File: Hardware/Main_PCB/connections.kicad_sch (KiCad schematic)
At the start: 6 parts, among them J701 Conn_01x08_Pin, J702 Conn_01x03_Pin, J703 Servo con, U701 NRF24L01, U702 SN74LV1T34DBV

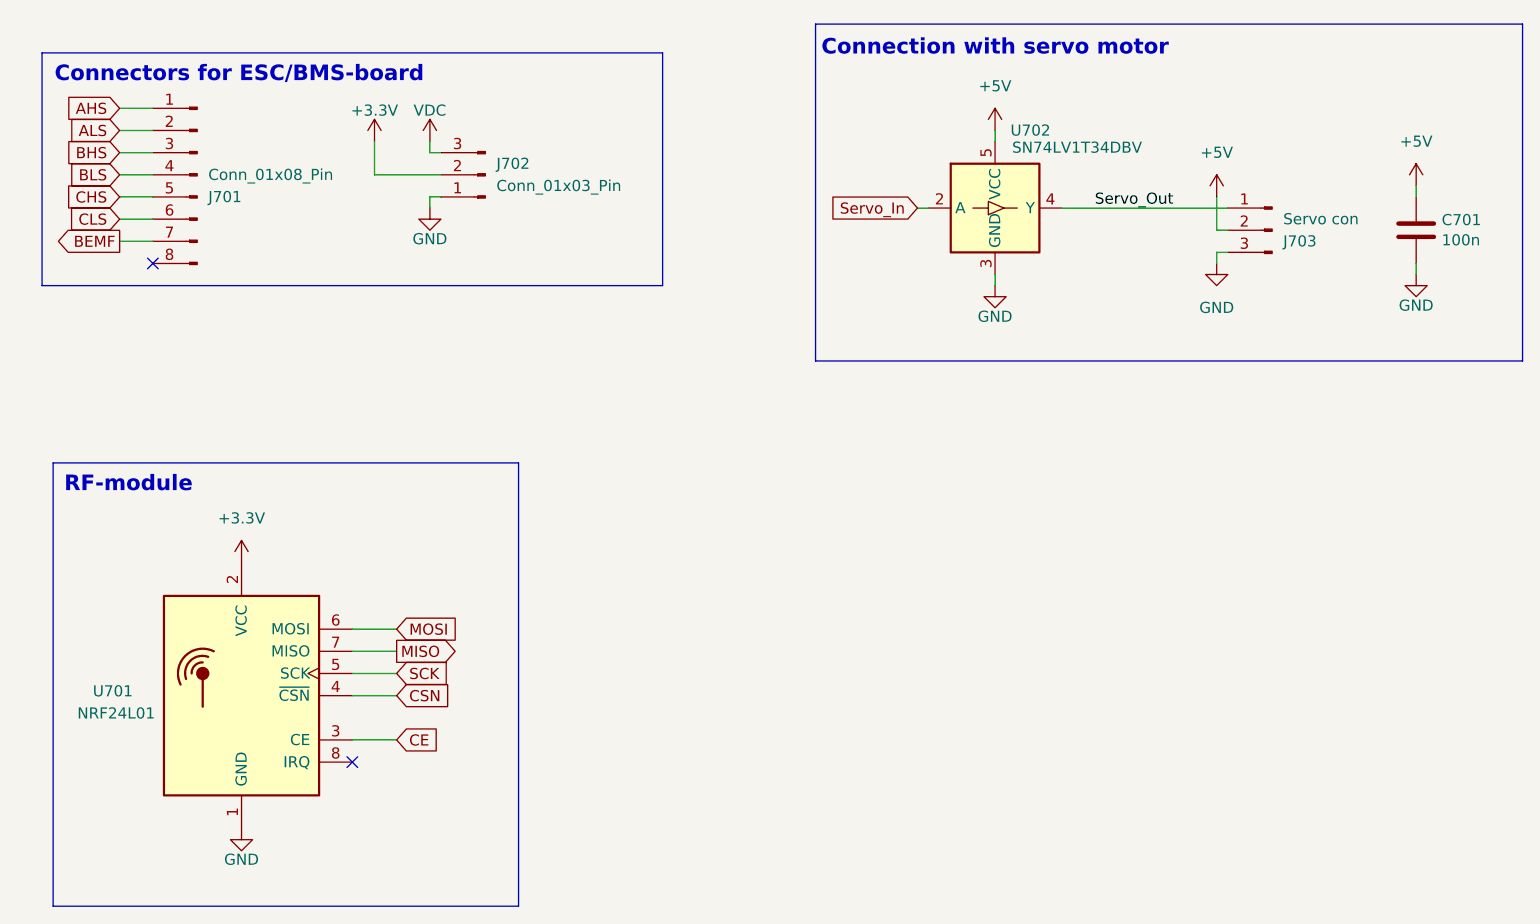
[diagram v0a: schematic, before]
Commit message: Added footprints to all components
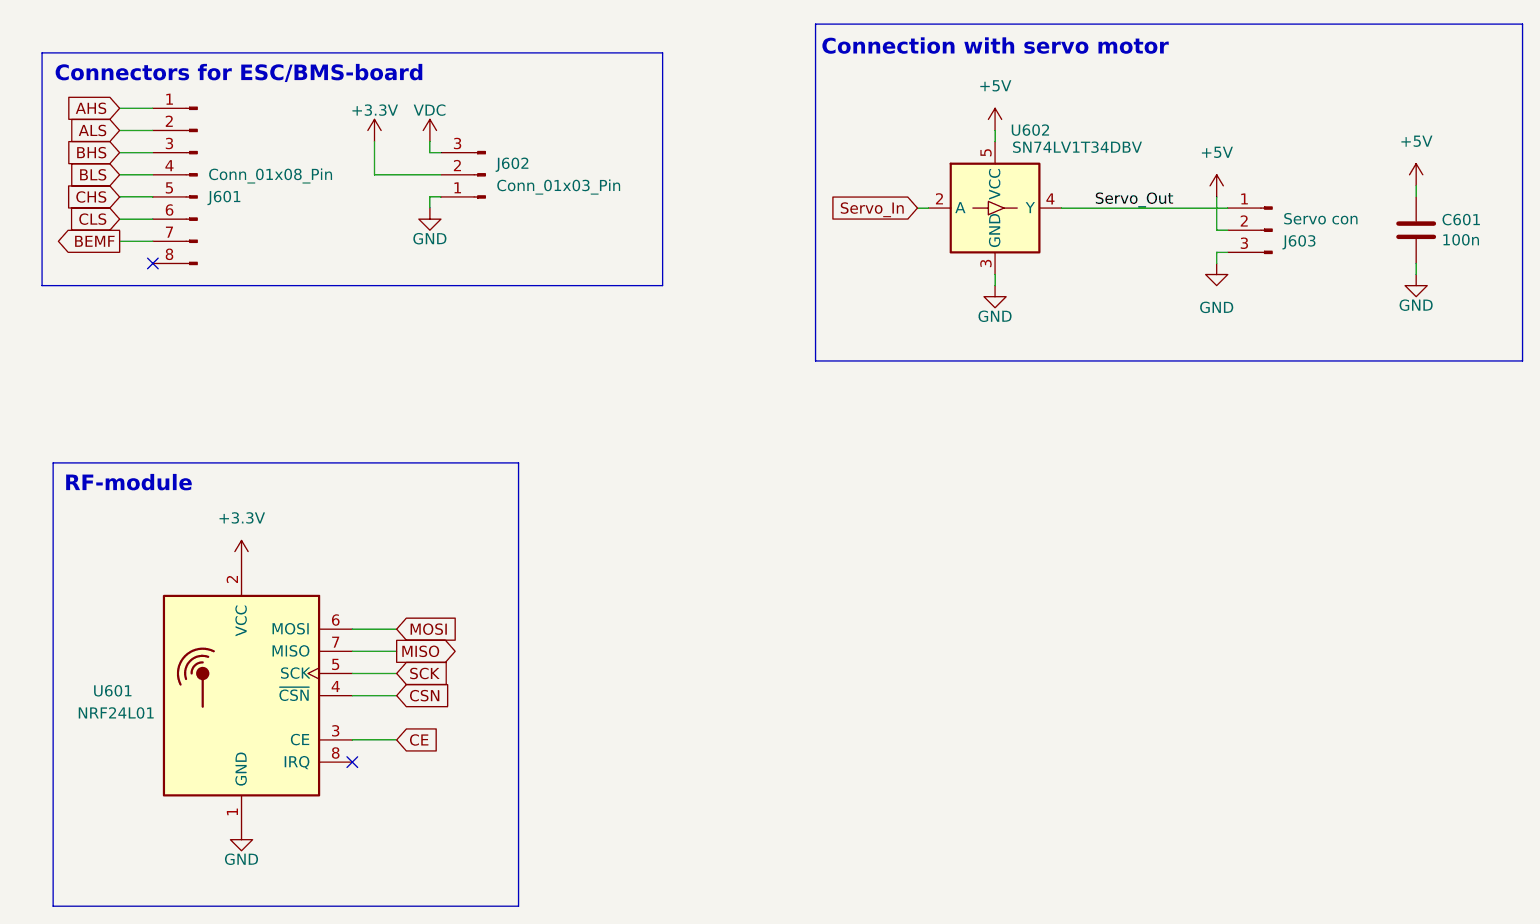
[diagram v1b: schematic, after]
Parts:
- renumbered C701 to C601, J701 to J601, J702 to J602, J703 to J603, U701 to U601, U702 to U602
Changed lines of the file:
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@@
 		(on_board yes)
 		(dnp no)
-		(property "Reference" "#PWR0707"
+		(property "Reference" "#PWR0607"
 			(at 130.81 54.61 0)
 			(effects
@@
 			(project "Main_PCB"
 				(path "/90d7beec-e1a2-46f8-bbb2-6b8f3489db10/2fd609f6-122d-440e-b3d6-5f283f47ac3b"
-					(reference "#PWR0707")
+					(reference "#PWR0607")
 					(unit 1)
 				)
@@
 		(dnp no)
 		(fields_autoplaced yes)
-		(property "Reference" "#PWR0709"
+		(property "Reference" "#PWR0609"
 			(at 156.21 52.07 0)
 			(effects
@@
 			(project "Main_PCB"
 				(path "/90d7beec-e1a2-46f8-bbb2-6b8f3489db10/2fd609f6-122d-440e-b3d6-5f283f47ac3b"
-					(reference "#PWR0709")
+					(reference "#PWR0609")
 					(unit 1)
 				)
@@
 		(dnp no)
 		(fields_autoplaced yes)
-		(property "Reference" "#PWR0710"
+		(property "Reference" "#PWR0610"
 			(at 179.07 40.64 0)
 			(effects
@@
 			(project "Main_PCB"
 				(path "/90d7beec-e1a2-46f8-bbb2-6b8f3489db10/2fd609f6-122d-440e-b3d6-5f283f47ac3b"
-					(reference "#PWR0710")
+					(reference "#PWR0610")
 					(unit 1)
 				)
@@
 		(on_board yes)
 		(dnp no)
-		(property "Reference" "J701"
+		(property "Reference" "J601"
 			(at 40.64 38.1001 0)
 			(effects
@@
 			(project "Main_PCB"
 				(path "/90d7beec-e1a2-46f8-bbb2-6b8f3489db10/2fd609f6-122d-440e-b3d6-5f283f47ac3b"
-					(reference "J701")
+					(reference "J601")
 					(unit 1)
 				)
@@
 		(on_board yes)
 		(dnp no)
-		(property "Reference" "U701"
+		(property "Reference" "U601"
 			(at 32.004 94.742 0)
 			(effects
@@
 			(project "Main_PCB"
 				(path "/90d7beec-e1a2-46f8-bbb2-6b8f3489db10/2fd609f6-122d-440e-b3d6-5f283f47ac3b"
-					(reference "U701")
+					(reference "U601")
 					(unit 1)
 				)
@@
 		(on_board yes)
 		(dnp no)
-		(property "Reference" "#PWR0702"
+		(property "Reference" "#PWR0602"
 			(at 44.45 116.84 0)
 			(effects
@@
 			(project "Main_PCB"
 				(path "/90d7beec-e1a2-46f8-bbb2-6b8f3489db10/2fd609f6-122d-440e-b3d6-5f283f47ac3b"
-					(reference "#PWR0702")
+					(reference "#PWR0602")
 					(unit 1)
 				)
@@
 		(on_board yes)
 		(dnp no)
-		(property "Reference" "#PWR0705"
+		(property "Reference" "#PWR0605"
 			(at 66.04 45.72 0)
 			(effects
@@
 			(project "Main_PCB"
 				(path "/90d7beec-e1a2-46f8-bbb2-6b8f3489db10/2fd609f6-122d-440e-b3d6-5f283f47ac3b"
-					(reference "#PWR0705")
+					(reference "#PWR0605")
 					(unit 1)
 				)
@@
 		(on_board yes)
 		(dnp no)
-		(property "Reference" "U702"
+		(property "Reference" "U602"
 			(at 134.874 30.48 0)
 			(effects
@@
 			(project "Main_PCB"
 				(path "/90d7beec-e1a2-46f8-bbb2-6b8f3489db10/2fd609f6-122d-440e-b3d6-5f283f47ac3b"
-					(reference "U702")
+					(reference "U602")
 					(unit 1)
 				)
@@
 		(on_board yes)
 		(dnp no)
-		(property "Reference" "C701"
+		(property "Reference" "C601"
 			(at 181.991 40.7416 0)
 			(effects
@@
 			(project "Main_PCB"
 				(path "/90d7beec-e1a2-46f8-bbb2-6b8f3489db10/2fd609f6-122d-440e-b3d6-5f283f47ac3b"
-					(reference "C701")
+					(reference "C601")
 					(unit 1)
 				)
@@
 		(on_board yes)
 		(dnp no)
-		(property "Reference" "#PWR0704"
+		(property "Reference" "#PWR0604"
 			(at 66.04 35.56 0)
 			(effects
@@
 			(project "Main_PCB"
 				(path "/90d7beec-e1a2-46f8-bbb2-6b8f3489db10/2fd609f6-122d-440e-b3d6-5f283f47ac3b"
-					(reference "#PWR0704")
+					(reference "#PWR0604")
 					(unit 1)
 				)
@@
 		(on_board yes)
 		(dnp no)
-		(property "Reference" "J703"
+		(property "Reference" "J603"
 			(at 163.83 43.1801 0)
 			(effects
@@
 			(project "Main_PCB"
 				(path "/90d7beec-e1a2-46f8-bbb2-6b8f3489db10/2fd609f6-122d-440e-b3d6-5f283f47ac3b"
-					(reference "J703")
+					(reference "J603")
 					(unit 1)
 				)
@@
 		(dnp no)
 		(fields_autoplaced yes)
-		(property "Reference" "#PWR0701"
+		(property "Reference" "#PWR0601"
 			(at 44.45 83.82 0)
 			(effects
@@
 			(project "Main_PCB"
 				(path "/90d7beec-e1a2-46f8-bbb2-6b8f3489db10/2fd609f6-122d-440e-b3d6-5f283f47ac3b"
-					(reference "#PWR0701")
+					(reference "#PWR0601")
 					(unit 1)
 				)
@@
 		(dnp no)
 		(fields_autoplaced yes)
-		(property "Reference" "#PWR0708"
+		(property "Reference" "#PWR0608"
 			(at 156.21 41.91 0)
 			(effects
@@
 			(project "Main_PCB"
 				(path "/90d7beec-e1a2-46f8-bbb2-6b8f3489db10/2fd609f6-122d-440e-b3d6-5f283f47ac3b"
-					(reference "#PWR0708")
+					(reference "#PWR0608")
 					(unit 1)
 				)
@@
 		(dnp no)
 		(fields_autoplaced yes)
-		(property "Reference" "#PWR0706"
+		(property "Reference" "#PWR0606"
 			(at 130.81 34.29 0)
 			(effects
@@
 			(project "Main_PCB"
 				(path "/90d7beec-e1a2-46f8-bbb2-6b8f3489db10/2fd609f6-122d-440e-b3d6-5f283f47ac3b"
-					(reference "#PWR0706")
+					(reference "#PWR0606")
 					(unit 1)
 				)
@@
 		(on_board yes)
 		(dnp no)
-		(property "Reference" "#PWR0703"
+		(property "Reference" "#PWR0603"
 			(at 59.69 35.56 0)
 			(effects
@@
 			(project "Main_PCB"
 				(path "/90d7beec-e1a2-46f8-bbb2-6b8f3489db10/2fd609f6-122d-440e-b3d6-5f283f47ac3b"
-					(reference "#PWR0703")
+					(reference "#PWR0603")
 					(unit 1)
 				)
@@
 		(on_board yes)
 		(dnp no)
-		(property "Reference" "#PWR0711"
+		(property "Reference" "#PWR0611"
 			(at 179.07 53.34 0)
 			(effects
@@
 			(project "Main_PCB"
 				(path "/90d7beec-e1a2-46f8-bbb2-6b8f3489db10/2fd609f6-122d-440e-b3d6-5f283f47ac3b"
-					(reference "#PWR0711")
+					(reference "#PWR0611")
 					(unit 1)
 				)
@@
 		(dnp no)
 		(fields_autoplaced yes)
-		(property "Reference" "J702"
+		(property "Reference" "J602"
 			(at 73.66 34.2899 0)
 			(effects
@@
 			(project "Main_PCB"
 				(path "/90d7beec-e1a2-46f8-bbb2-6b8f3489db10/2fd609f6-122d-440e-b3d6-5f283f47ac3b"
-					(reference "J702")
-					(unit 1)
-				)
+					(reference "J602")
+					(unit 1)
+				)

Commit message: Finished the schematic of the MainPCB
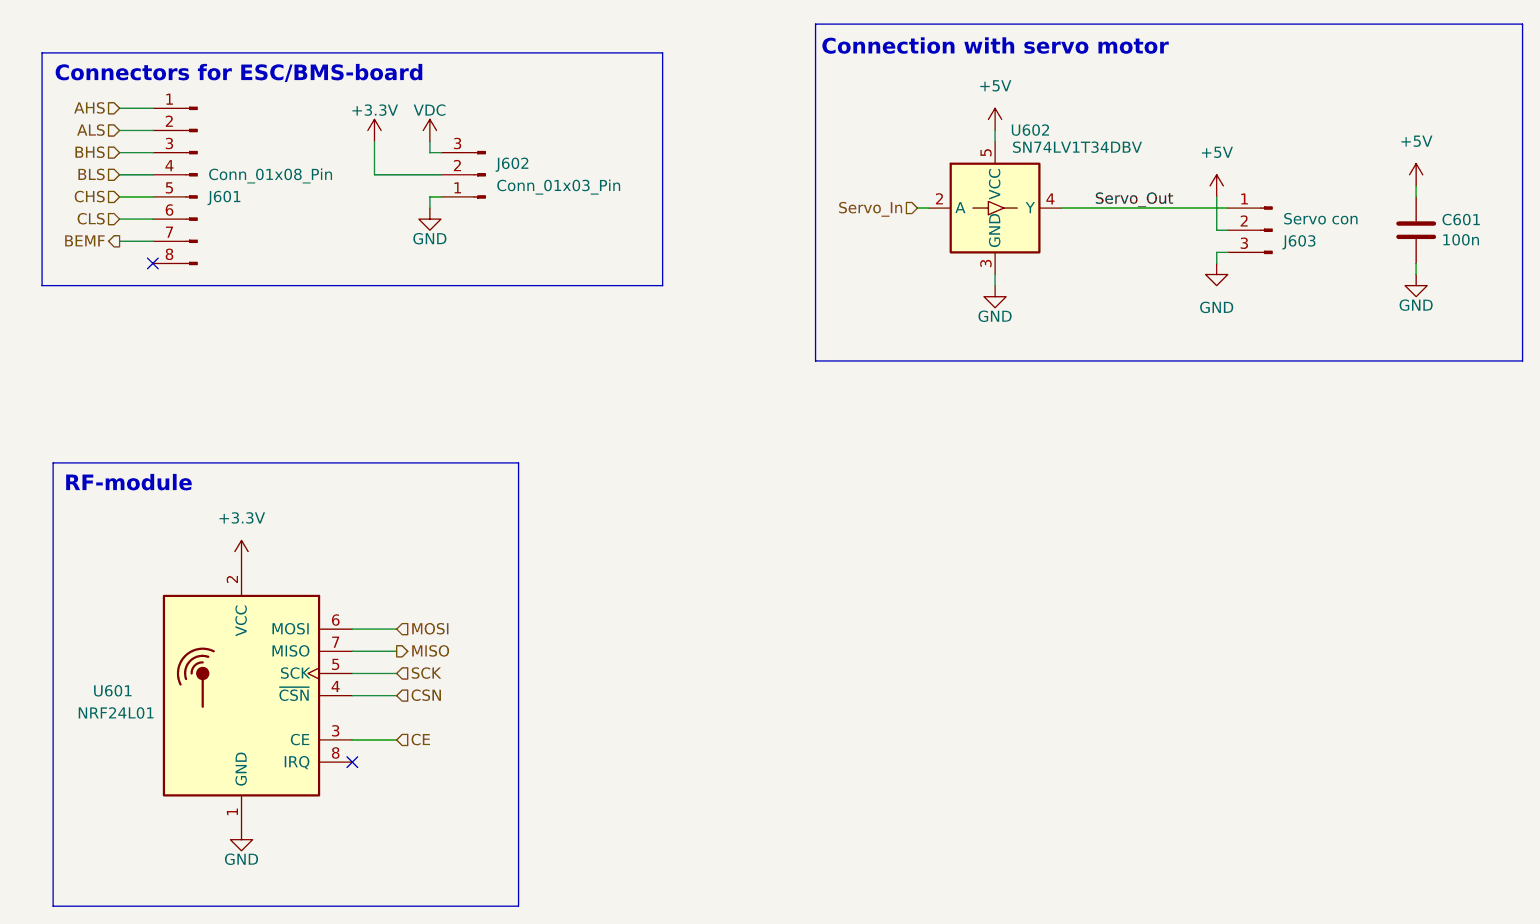
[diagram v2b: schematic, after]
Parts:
- U601: footprint RF_Module:nRF24L01_Breakout -> Connector_PinHeader_2.54mm:PinHeader_2x04_P2.54mm_Vertical
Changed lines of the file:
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@@
 		)
 	)
-	(global_label "CSN"
+	(hierarchical_label "CHS"
+		(shape input)
+		(at 30.48 38.1 180)
+		(effects
+			(font
+				(size 1.27 1.27)
+			)
+			(justify right)
+		)
+	)
+	(hierarchical_label "BHS"
+		(shape input)
+		(at 30.48 33.02 180)
+		(effects
+			(font
+				(size 1.27 1.27)
+			)
+			(justify right)
+		)
+	)
+	(hierarchical_label "AHS"
+		(shape input)
+		(at 30.48 27.94 180)
+		(effects
+			(font
+				(size 1.27 1.27)
+			)
+			(justify right)
+		)
+	)
+	(hierarchical_label "CE"
+		(shape input)
+		(at 62.23 100.33 0)
+		(effects
+			(font
+				(size 1.27 1.27)
+			)
+			(justify left)
+		)
+	)
+	(hierarchical_label "MOSI"
+		(shape input)
+		(at 62.23 87.63 0)
+		(effects
+			(font
+				(size 1.27 1.27)
+			)
+			(justify left)
+		)
+	)
+	(hierarchical_label "BLS"
+		(shape input)
+		(at 30.48 35.56 180)
+		(effects
+			(font
+				(size 1.27 1.27)
+			)
+			(justify right)
+		)
+	)
+	(hierarchical_label "Servo_In"
+		(shape input)
+		(at 121.92 39.37 180)
+		(effects
+			(font
+				(size 1.27 1.27)
+			)
+			(justify right)
+		)
+	)
+	(hierarchical_label "CSN"
 		(shape input)
 		(at 62.23 95.25 0)
-		(fields_autoplaced yes)
 		(effects
 			(font
@@
 			(justify left)
 		)
-		(property "Intersheetrefs" "${INTERSHEET_REFS}"
-			(at 69.0252 95.25 0)
-			(effects
-				(font
-					(size 1.27 1.27)
-				)
-				(justify left)
-				(hide yes)
-			)
-		)
-	)
-	(global_label "MOSI"
-		(shape input)
-		(at 62.23 87.63 0)
-		(fields_autoplaced yes)
-		(effects
-			(font
-				(size 1.27 1.27)
-				(thickness 0.1588)
+	)
+	(hierarchical_label "SCK"
+		(shape input)
+		(at 62.23 92.71 0)
+		(effects
+			(font
+				(size 1.27 1.27)
 			)
 			(justify left)
 		)
-		(property "Intersheetrefs" "${INTERSHEET_REFS}"
-			(at 69.8114 87.63 0)
-			(effects
-				(font
-					(size 1.27 1.27)
-				)
-				(justify left)
-				(hide yes)
-			)
-		)
-	)
-	(global_label "AHS"
-		(shape input)
-		(at 30.48 27.94 180)
-		(fields_autoplaced yes)
-		(effects
-			(font
-				(size 1.27 1.27)
-			)
-			(justify right)
-		)
-		(property "Intersheetrefs" "${INTERSHEET_REFS}"
-			(at 23.8662 27.94 0)
-			(effects
-				(font
-					(size 1.27 1.27)
-				)
-				(justify right)
-				(hide yes)
-			)
-		)
-	)
-	(global_label "BHS"
-		(shape input)
-		(at 30.48 33.02 180)
-		(fields_autoplaced yes)
-		(effects
-			(font
-				(size 1.27 1.27)
-			)
-			(justify right)
-		)
-		(property "Intersheetrefs" "${INTERSHEET_REFS}"
-			(at 23.6848 33.02 0)
-			(effects
-				(font
-					(size 1.27 1.27)
-				)
-				(justify right)
-				(hide yes)
-			)
-		)
-	)
-	(global_label "Servo_In"
-		(shape input)
-		(at 121.92 39.37 180)
-		(fields_autoplaced yes)
-		(effects
-			(font
-				(size 1.27 1.27)
-			)
-			(justify right)
-		)
-		(property "Intersheetrefs" "${INTERSHEET_REFS}"
-			(at 111.0125 39.37 0)
-			(effects
-				(font
-					(size 1.27 1.27)
-				)
-				(justify right)
-				(hide yes)
-			)
-		)
-	)
-	(global_label "CHS"
-		(shape input)
-		(at 30.48 38.1 180)
-		(fields_autoplaced yes)
-		(effects
-			(font
-				(size 1.27 1.27)
-			)
-			(justify right)
-		)
-		(property "Intersheetrefs" "${INTERSHEET_REFS}"
-			(at 23.6848 38.1 0)
-			(effects
-				(font
-					(size 1.27 1.27)
-				)
-				(justify right)
-				(hide yes)
-			)
-		)
-	)
-	(global_label "ALS"
+	)
+	(hierarchical_label "MISO"
+		(shape output)
+		(at 62.23 90.17 0)
+		(effects
+			(font
+				(size 1.27 1.27)
+			)
+			(justify left)
+		)
+	)
+	(hierarchical_label "CLS"
+		(shape input)
+		(at 30.48 40.64 180)
+		(effects
+			(font
+				(size 1.27 1.27)
+			)
+			(justify right)
+		)
+	)
+	(hierarchical_label "ALS"
 		(shape input)
 		(at 30.48 30.48 180)
-		(fields_autoplaced yes)
-		(effects
-			(font
-				(size 1.27 1.27)
-			)
-			(justify right)
-		)
-		(property "Intersheetrefs" "${INTERSHEET_REFS}"
-			(at 24.1686 30.48 0)
-			(effects
-				(font
-					(size 1.27 1.27)
-				)
-				(justify right)
-				(hide yes)
-			)
-		)
-	)
-	(global_label "BLS"
-		(shape input)
-		(at 30.48 35.56 180)
-		(fields_autoplaced yes)
-		(effects
-			(font
-				(size 1.27 1.27)
-			)
-			(justify right)
-		)
-		(property "Intersheetrefs" "${INTERSHEET_REFS}"
-			(at 23.9872 35.56 0)
-			(effects
-				(font
-					(size 1.27 1.27)
-				)
-				(justify right)
-				(hide yes)
-			)
-		)
-	)
-	(global_label "SCK"
-		(shape input)
-		(at 62.23 92.71 0)
-		(fields_autoplaced yes)
-		(effects
-			(font
-				(size 1.27 1.27)
-				(thickness 0.1588)
-			)
-			(justify left)
-		)
-		(property "Intersheetrefs" "${INTERSHEET_REFS}"
-			(at 68.9647 92.71 0)
-			(effects
-				(font
-					(size 1.27 1.27)
-				)
-				(justify left)
-				(hide yes)
-			)
-		)
-	)
-	(global_label "CE"
-		(shape input)
-		(at 62.23 100.33 0)
-		(fields_autoplaced yes)
-		(effects
-			(font
-				(size 1.27 1.27)
-			)
-			(justify left)
-		)
-		(property "Intersheetrefs" "${INTERSHEET_REFS}"
-			(at 67.6342 100.33 0)
-			(effects
-				(font
-					(size 1.27 1.27)
-				)
-				(justify left)
-				(hide yes)
-			)
-		)
-	)
-	(global_label "BEMF"
+		(effects
+			(font
+				(size 1.27 1.27)
+			)
+			(justify right)
+		)
+	)
+	(hierarchical_label "BEMF"
 		(shape output)
 		(at 30.48 43.18 180)
-		(fields_autoplaced yes)
-		(effects
-			(font
-				(size 1.27 1.27)
-			)
-			(justify right)
-		)
-		(property "Intersheetrefs" "${INTERSHEET_REFS}"
-			(at 22.5358 43.18 0)
-			(effects
-				(font
-					(size 1.27 1.27)
-				)
-				(justify right)
-				(hide yes)
-			)
-		)
-	)
-	(global_label "CLS"
-		(shape input)
-		(at 30.48 40.64 180)
-		(fields_autoplaced yes)
-		(effects
-			(font
-				(size 1.27 1.27)
-			)
-			(justify right)
-		)
-		(property "Intersheetrefs" "${INTERSHEET_REFS}"
-			(at 23.9872 40.64 0)
-			(effects
-				(font
-					(size 1.27 1.27)
-				)
-				(justify right)
-				(hide yes)
-			)
-		)
-	)
-	(global_label "MISO"
-		(shape output)
-		(at 62.23 90.17 0)
-		(fields_autoplaced yes)
-		(effects
-			(font
-				(size 1.27 1.27)
-				(thickness 0.1588)
-			)
-			(justify left)
-		)
-		(property "Intersheetrefs" "${INTERSHEET_REFS}"
-			(at 69.8114 90.17 0)
-			(effects
-				(font
-					(size 1.27 1.27)
-				)
-				(justify left)
-				(hide yes)
-			)
+		(effects
+			(font
+				(size 1.27 1.27)
+			)
+			(justify right)
 		)
 	)
@@
 			)
 		)
-		(property "Footprint" "RF_Module:nRF24L01_Breakout"
+		(property "Footprint" "Connector_PinHeader_2.54mm:PinHeader_2x04_P2.54mm_Vertical"
 			(at 40.64 80.01 0)
 			(effects

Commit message: Probably a final version of the MAIN PCB component placement
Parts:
- U601: footprint Connector_PinHeader_2.54mm:PinHeader_2x04_P2.54mm_Vertical -> Connector_PinSocket_2.54mm:PinSocket_2x04_P2.54mm_Vertical
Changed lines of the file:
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@@
 			)
 		)
-		(property "Footprint" "Connector_PinHeader_2.54mm:PinHeader_2x04_P2.54mm_Vertical"
+		(property "Footprint" "Connector_PinSocket_2.54mm:PinSocket_2x04_P2.54mm_Vertical"
 			(at 40.64 80.01 0)
 			(effects
